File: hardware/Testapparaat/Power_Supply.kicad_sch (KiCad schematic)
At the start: 2 parts

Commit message: -enh Made the schematic for the main unit almost complete :)
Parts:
- removed BT?: Li-battery 3,5-4,2V, symbol Device:Battery
- removed M?: TP4056_Module, testapparaat_footprint:4056E_LiIon_Charger, symbol testapparaat_symbols:TP4056_Module
- added BT1: NIMH_CELL_AA_1, symbol Device:Battery_Cell
- added BT2: NIMH_CELL_AA_8, symbol Device:Battery_Cell
- added BT3: NIMH_CELL_AA_2, symbol Device:Battery_Cell
- added BT4: NIMH_CELL_AA_7, symbol Device:Battery_Cell
- added BT5: NIMH_CELL_AA_6, symbol Device:Battery_Cell
- added BT6: NIMH_CELL_AA_3, symbol Device:Battery_Cell
- added BT7: NIMH_CELL_AA_4, symbol Device:Battery_Cell
- added BT8: NIMH_CELL_AA_5, symbol Device:Battery_Cell
- added C2: 220u, symbol Device:C_Polarized
- added C3: 1u, symbol Device:C
- added C4, C5: 100n, symbol Device:C
- added C6, C7: 2.2u, symbol Device:C
- added C8, C9: 10u, symbol Device:C_Polarized
- added F1: F2.5A GLASS, symbol Device:Fuse
- added L1: 4.7uH, symbol Device:L
- added L2: 3.3uH, symbol Device:L
- added PS1, PS2: LMR50410YFQDBVRQ1, LMR50410YFQDBVRQ1:SOT95P280X145-6N, symbol LMR50410YFQDBVRQ1:LMR50410YFQDBVRQ1
- added R10: 20k, symbol Device:R
- added R6: 100k, symbol Device:R
- added R7: 91k, symbol Device:R
- added R8: 22k, symbol Device:R
- added R9: 43k, symbol Device:R
- added SW2: on/off switch, symbol Switch:SW_Push_SPDT
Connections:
- net 3.3V_OUT: now also C9.1, L2.2, R9.1
- net 5V_OUT: now also C8.1, L1.2, R7.1
- new net: PS1.3 (FB), R7.2, R8.1
- new net: BT6.1 (+), BT7.1 (+)
- new net: BT3.1 (+), BT6.2 (-)
- new net: PS2.3 (FB), R10.1, R9.2
- new net: BT2.1 (+), C2.1, F1.2
- new net: BT4.2 (-), BT5.1 (+)
- new net: BT5.2 (-), BT8.1 (+)
- new net: C4.1, L1.1, PS1.6 (SW)
- new net: BT7.2 (-), BT8.2 (-)
- new net: C4.2, PS1.1 (CB)
- new net: BT1.1 (+), BT3.2 (-)
- new net: BT2.2 (-), BT4.1 (+)
- new net: C5.2, PS2.1 (CB)
- new net: C5.1, L2.1, PS2.6 (SW)
- new net BATT_OUT+: C6.1, C7.1, F1.1, PS1.5 (VIN), PS2.5 (VIN), SW2.1 (A)
- new net BATT_OUT-: BT1.2 (-), C2.2, C3.2, C6.2, C7.2, C8.2, C9.2, PS1.2 (GND), PS2.2 (GND), R10.2, R6.2, R8.2, SW2.3 (C)
- new net REG_EN: C3.1, PS1.4 (EN), PS2.4 (EN), R6.1, SW2.2 (B)
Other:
- note added: "RFBT = ((Vout-Vref)/Vref)*RFBB RFBB = 20k (gaf een goede verhouding) Vref = 1v (datasheet LMR) RFBT = ((3.2-1)/1)*20000 = 44k -> 43k gekozen"
- note added: "RFBT = ((Vout-Vref)/Vref)*RFBB RFBB = 22k (gaf een goede verhouding) Vref = 1v (datasheet LMR) RFBT = ((5.2-1)/1)*20000=92,4k -> 91k gekozen"

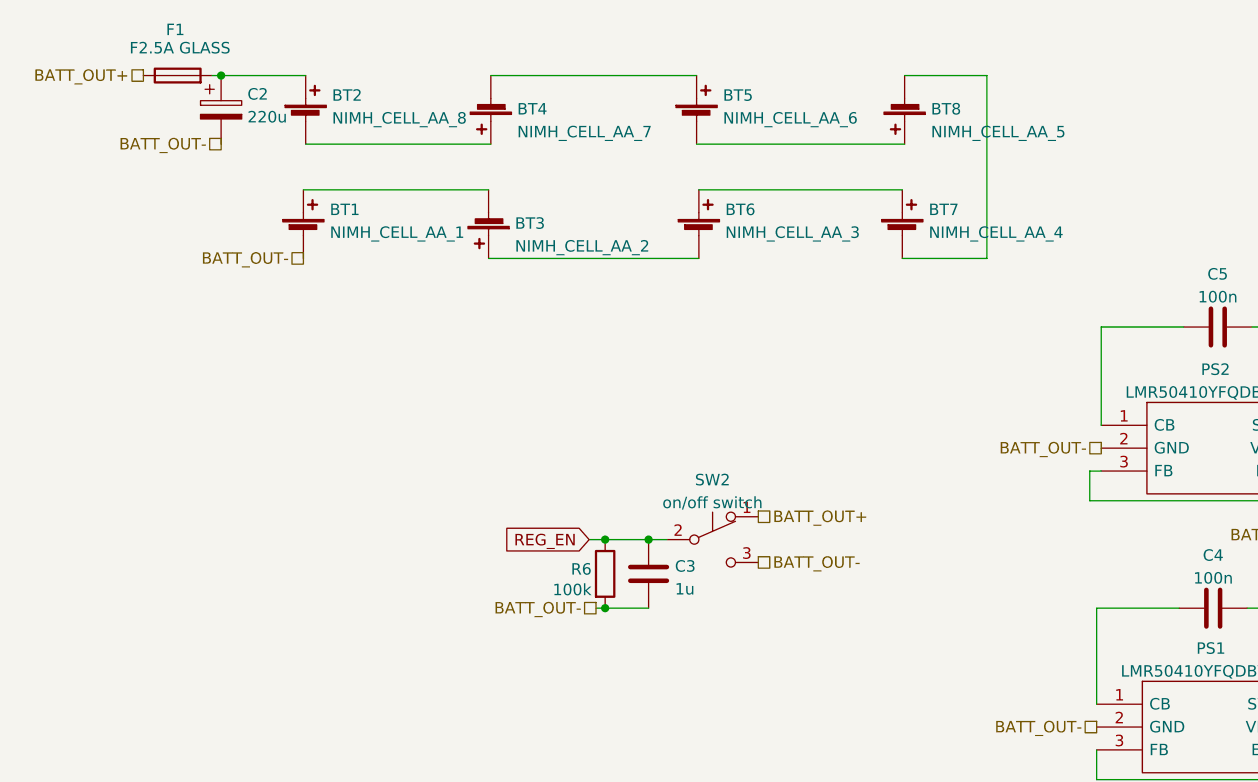
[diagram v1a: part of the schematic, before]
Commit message: -enh Noodstop is now hardware controlled
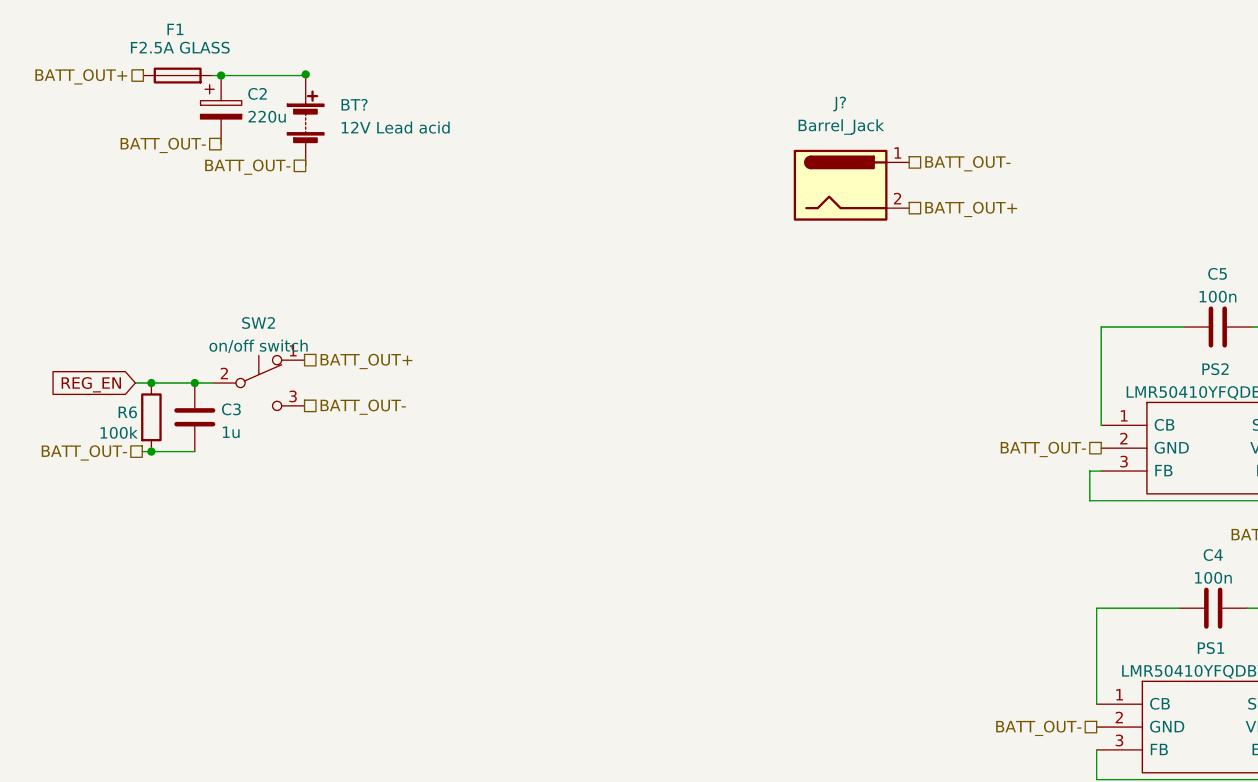
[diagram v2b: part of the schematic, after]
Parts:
- removed BT1: NIMH_CELL_AA_1, symbol Device:Battery_Cell
- removed BT2: NIMH_CELL_AA_8, symbol Device:Battery_Cell
- removed BT3: NIMH_CELL_AA_2, symbol Device:Battery_Cell
- removed BT4: NIMH_CELL_AA_7, symbol Device:Battery_Cell
- removed BT5: NIMH_CELL_AA_6, symbol Device:Battery_Cell
- removed BT6: NIMH_CELL_AA_3, symbol Device:Battery_Cell
- removed BT7: NIMH_CELL_AA_4, symbol Device:Battery_Cell
- removed BT8: NIMH_CELL_AA_5, symbol Device:Battery_Cell
- added BT?: 12V Lead acid, symbol Device:Battery
- added J?: Barrel_Jack, symbol Connector:Barrel_Jack
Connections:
- net BATT_OUT+: now also J?.2
- net BATT_OUT-: now also BT?.2 (-), J?.1
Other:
- moved on the sheet: C3, R6, SW2

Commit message: -enh made some changes to schematic and assigned fp
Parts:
- added D8: 1N5401, Diode_THT:D_DO-201AD_P15.24mm_Horizontal, symbol Diode:1N5401
- added J10: B-, TestPoint:TestPoint_Plated_Hole_D2.0mm, symbol Connector:Conn_01x01_Female
- added J9: B+, TestPoint:TestPoint_Plated_Hole_D2.0mm, symbol Connector:Conn_01x01_Female
- C2: footprint (none) -> Capacitor_THT:C_Radial_D10.0mm_H12.5mm_P5.00mm
- C3, C4, C5, C6, C7, C8, C9: footprint (none) -> Capacitor_SMD:C_0603_1608Metric_Pad1.08x0.95mm_HandSolder
- F1: footprint (none) -> Fuse:Fuseholder_Blade_ATO_Littelfuse_Pudenz_2_Pin
- J8: renamed from J?; footprint (none) -> Connector_BarrelJack:BarrelJack_Wuerth_6941xx301002
- L1, L2: footprint (none) -> Inductor_SMD:L_Bourns-SRU8028_8.0x8.0mm
- R10, R6, R7, R8, R9: footprint (none) -> Resistor_SMD:R_0603_1608Metric_Pad0.98x0.95mm_HandSolder
- SW2: footprint (none) -> Button_Switch_THT:SW_Slide_1P2T_CK_OS102011MS2Q
- gave numbers to parts that had none: 1
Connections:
- net BATT_OUT+: now also D8.1 (K); no longer J8.2
- net BATT_OUT-: now also J8.2, J10.1 (Pin_1); no longer J8.1
- net at C2.1, F1.2: now also J9.1 (Pin_1)
- new net: D8.2 (A), J8.1

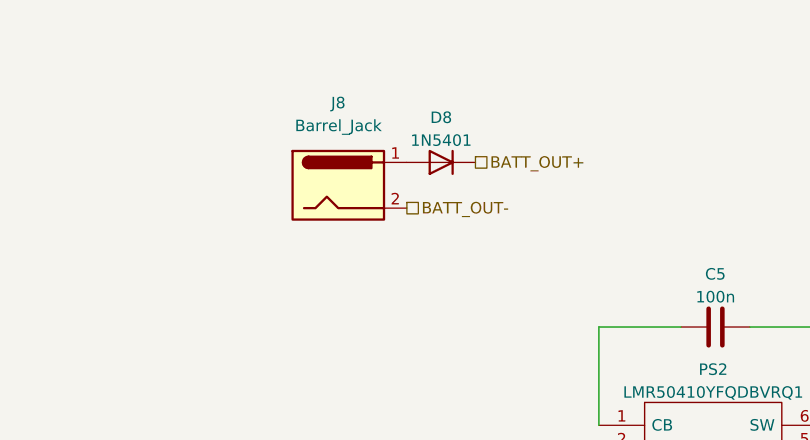
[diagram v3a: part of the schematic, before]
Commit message: -enh add seperate schematic and pcb for io ports/slots
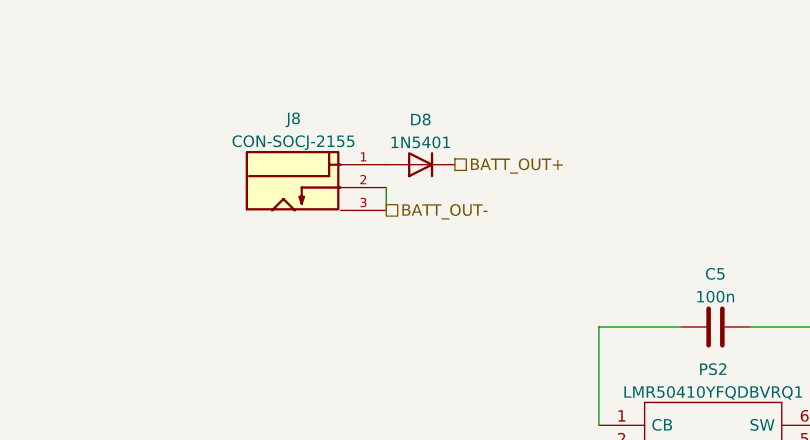
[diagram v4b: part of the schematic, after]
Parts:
- removed J8: Barrel_Jack, Connector_BarrelJack:BarrelJack_Wuerth_6941xx301002, symbol Connector:Barrel_Jack
- added J8: CON-SOCJ-2155, Barrel_jack:GRAVITECH_CON-SOCJ-2155, symbol Barrel_jack:CON-SOCJ-2155
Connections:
- net BATT_OUT-: now also J8.2, J8.3
- net at D8.2 (A): now also J8.1
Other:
- moved on the sheet: D8
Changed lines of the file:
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@@
+    (stroke (width 0) (type default) (color 0 0 0 0))
+  )
+  (wire (pts (xy 121.92 30.988) (xy 121.92 33.528))
     (stroke (width 0) (type default) (color 0 0 0 0))
   )
@@
     (effects (font (size 1.27 1.27)) (justify right))
   )
-  (hierarchical_label "BATT_OUT+" (shape passive) (at 131.826 28.194 0)
+  (hierarchical_label "BATT_OUT+" (shape passive) (at 129.54 28.448 0)
     (effects (font (size 1.27 1.27)) (justify left))
   )
@@
     (effects (font (size 1.27 1.27)) (justify left))
   )
-  (hierarchical_label "BATT_OUT-" (shape passive) (at 124.206 33.274 0)
+  (hierarchical_label "BATT_OUT-" (shape passive) (at 121.92 33.528 0)
     (effects (font (size 1.27 1.27)) (justify left))
   )
@@
     (pin "1")
   )
-  (symbol (lib_id "Diode:1N5401") (at 128.016 28.194 180) (unit 1)
-    (in_bom yes) (on_board yes) (fields_autoplaced)
-    (property "Reference" "D8" (id 0) (at 128.016 23.2242 0))
-    (property "Value" "1N5401" (id 1) (at 128.016 25.7611 0))
-    (property "Footprint" "Diode_THT:D_DO-201AD_P15.24mm_Horizontal" (id 2) (at 128.016 23.749 0)
-      (effects (font (size 1.27 1.27)) hide)
-    )
-    (property "Datasheet" "http://www.vishay.com/docs/88516/1n5400.pdf" (id 3) (at 128.016 28.194 0)
-      (effects (font (size 1.27 1.27)) hide)
-    )
-    (pin "1")
-    (pin "2")
+  (symbol (lib_id "Diode:1N5401") (at 125.73 28.448 180) (unit 1)
+    (in_bom yes) (on_board yes) (fields_autoplaced)
+    (property "Reference" "D8" (id 0) (at 125.73 23.4782 0))
+    (property "Value" "1N5401" (id 1) (at 125.73 26.0151 0))
+    (property "Footprint" "Diode_THT:D_DO-201AD_P15.24mm_Horizontal" (id 2) (at 125.73 24.003 0)
+      (effects (font (size 1.27 1.27)) hide)
+    )
+    (property "Datasheet" "http://www.vishay.com/docs/88516/1n5400.pdf" (id 3) (at 125.73 28.448 0)
+      (effects (font (size 1.27 1.27)) hide)
+    )
+    (pin "1")
+    (pin "2")
+  )
+  (symbol (lib_id "Barrel_jack:CON-SOCJ-2155") (at 111.76 30.988 0) (unit 1)
+    (in_bom yes) (on_board yes) (fields_autoplaced)
+    (property "Reference" "J8" (id 0) (at 111.633 23.3512 0))
+    (property "Value" "CON-SOCJ-2155" (id 1) (at 111.633 25.8881 0))
+    (property "Footprint" "Barrel_jack:GRAVITECH_CON-SOCJ-2155" (id 2) (at 111.76 30.988 0)
+      (effects (font (size 1.27 1.27)) (justify left bottom) hide)
+    )
+    (property "Datasheet" "" (id 3) (at 111.76 30.988 0)
+      (effects (font (size 1.27 1.27)) (justify left bottom) hide)
+    )
+    (property "STANDARD" "Manufacturer Recommendations" (id 4) (at 111.76 30.988 0)
+      (effects (font (size 1.27 1.27)) (justify left bottom) hide)
+    )
+    (property "PARTREV" "NA" (id 5) (at 111.76 30.988 0)
+      (effects (font (size 1.27 1.27)) (justify left bottom) hide)
+    )
+    (property "MANUFACTURER" "Gravitech" (id 6) (at 111.76 30.988 0)
+      (effects (font (size 1.27 1.27)) (justify left bottom) hide)
+    )
+    (property "MAXIMUM_PACKAGE_HEIGHT" "11.1 mm" (id 7) (at 111.76 30.988 0)
+      (effects (font (size 1.27 1.27)) (justify left bottom) hide)
+    )
+    (pin "1")
+    (pin "2")
+    (pin "3")
   )
   (symbol (lib_id "Connector:Conn_01x01_Female") (at 62.23 18.542 0) (unit 1)
@@
       (effects (font (size 1.27 1.27)) hide)
     )
-    (pin "1")
-    (pin "2")
-  )
-  (symbol (lib_id "Connector:Barrel_Jack") (at 116.586 30.734 0) (unit 1)
-    (in_bom yes) (on_board yes) (fields_autoplaced)
-    (property "Reference" "J8" (id 0) (at 116.586 21.59 0))
-    (property "Value" "Barrel_Jack" (id 1) (at 116.586 24.13 0))
-    (property "Footprint" "Connector_BarrelJack:BarrelJack_Wuerth_6941xx301002" (id 2) (at 117.856 31.75 0)
-      (effects (font (size 1.27 1.27)) hide)
-    )
-    (property "Datasheet" "~" (id 3) (at 117.856 31.75 0)
-      (effects (font (size 1.27 1.27)) hide)
-    )

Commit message: -add bom and new schematic
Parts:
- removed C4, C5: 100n, Capacitor_SMD:C_0603_1608Metric_Pad1.08x0.95mm_HandSolder, symbol Device:C
- removed C7: 2.2u, Capacitor_SMD:C_0603_1608Metric_Pad1.08x0.95mm_HandSolder, symbol Device:C
- removed PS1, PS2: LMR50410YFQDBVRQ1, LMR50410YFQDBVRQ1:SOT95P280X145-6N, symbol LMR50410YFQDBVRQ1:LMR50410YFQDBVRQ1
- added D? (x2): SS310, symbol Device:D_Schottky
- added U? (x2): LM2596S-ADJ, Package_TO_SOT_SMD:TO-263-5_TabPin3, symbol Regulator_Switching:LM2596S-ADJ
- C8, C9: value 10u -> 220u
- L1: value 4.7uH -> 68uH
- L2: value 3.3uH -> 68uH
- R10: value 20k -> 1k
- R7: value 91k -> 680
- R8: value 22k -> 220
- R9: value 43k -> 1,6k
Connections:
- net BATT_OUT+: now also U?.1 (VIN), U?.1 (VIN)
- net BATT_OUT-: now also D?.2 (A), D?.2 (A), U?.3 (GND), U?.3 (GND)
- net REG_EN: now also U?.5 (~{ON}/OFF), U?.5 (~{ON}/OFF)
- net at R7.2, R8.1: now also U?.4 (FB)
- net at R10.1, R9.2: now also U?.4 (FB)
- net at L1.1: now also D?.1 (K), U?.2 (OUT)
- net at L2.1: now also D?.1 (K), U?.2 (OUT)
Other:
- note added: "RFBT = RFBB((vout/vref)-1) RFBB = 1k (gaf een goede verhouding) Vref = 1,23v (datasheet LM2596) RFBT = 1k((3,3/1,23)-1)= 1,68k -> 1,6k gekozen"
- note added: "RFBT = RFBB((vout/vref)-1) RFBB = 1k (gaf een goede verhouding) Vref = 1,23v (datasheet LM2596) RFBT = 1k((5/1,23)-1)= 3065R -> 3k gekozen"
- note removed: "RFBT = ((Vout-Vref)/Vref)*RFBB RFBB = 20k (gaf een goede verhouding) Vref = 1v (datasheet LMR) RFBT = ((3.2-1)/1)*20000 = 44k -> 43k gekozen"
- note removed: "RFBT = ((Vout-Vref)/Vref)*RFBB RFBB = 22k (gaf een goede verhouding) Vref = 1v (datasheet LMR) RFBT = ((5.2-1)/1)*20000=92,4k -> 91k gekozen"
- moved on the sheet: C6

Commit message: -enh Made a start at pcb design
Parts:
- removed C6: 2.2u, Capacitor_SMD:C_0603_1608Metric_Pad1.08x0.95mm_HandSolder, symbol Device:C
- removed D8: 1N5401, Diode_THT:D_DO-201AD_P15.24mm_Horizontal, symbol Diode:1N5401
- removed U? (x2): LM2596S-ADJ, Package_TO_SOT_SMD:TO-263-5_TabPin3, symbol Regulator_Switching:LM2596S-ADJ
- added D4: SS310, Diode_SMD:D_SMA_Handsoldering, symbol Device:D_Schottky
- added U10: LM2596S-5, Package_TO_SOT_SMD:TO-263-5_TabPin3, symbol Regulator_Switching:LM2596S-5
- added U11: LM2596S-3.3, Package_TO_SOT_SMD:TO-263-5_TabPin3, symbol Regulator_Switching:LM2596S-3.3
- C8, C9: footprint Capacitor_SMD:C_0603_1608Metric_Pad1.08x0.95mm_HandSolder -> Capacitor_THT:C_Radial_D10.0mm_H12.5mm_P5.00mm
- D1, D2: renamed from D?; footprint (none) -> Diode_SMD:D_SMA_Handsoldering
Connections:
- net REG_EN: now also U10.5 (~{ON}/OFF), U11.5 (~{ON}/OFF)
- net at R7.2, R8.1: now also U10.4 (FB)
- net at R10.1, R9.2: now also U11.4 (FB)
- net at C2.1, F1.2, J9.1 (Pin_1): now also #BT1.1 (+)
- net at D1.1 (K), L1.1: now also U10.2 (OUT)
- net at D2.1 (K), L2.1: now also U11.2 (OUT)
- net at J8.1: now also D4.2 (A)
- net 3.3V_OUT renamed +3.3V
- net 5V_OUT renamed +5V
- net BATT_OUT+ renamed +BATT
- net +BATT: now also D4.1 (K), U10.1 (VIN), U11.1 (VIN)
- net BATT_OUT- renamed GND
- net GND: now also U10.3 (GND), U11.3 (GND)
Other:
- moved on the sheet: C2, F1, J10, J9

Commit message: -enh First look at layout, proposed it to the team
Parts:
- F1: footprint Fuse:Fuseholder_Blade_ATO_Littelfuse_Pudenz_2_Pin -> Fuse:Fuseholder_Littelfuse_100_series_5x20mm
- L1, L2: footprint Inductor_SMD:L_Bourns-SRU8028_8.0x8.0mm -> srr1260:SRR1260-680M
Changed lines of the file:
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@@
     (property "Reference" "F1" (id 0) (at 67.564 13.462 90))
     (property "Value" "F2.5A GLASS" (id 1) (at 67.056 15.494 90))
-    (property "Footprint" "Fuse:Fuseholder_Blade_ATO_Littelfuse_Pudenz_2_Pin" (id 2) (at 67.31 20.32 90)
+    (property "Footprint" "Fuse:Fuseholder_Littelfuse_100_series_5x20mm" (id 2) (at 67.31 20.32 90)
       (effects (font (size 1.27 1.27)) hide)
     )
@@
     (property "Reference" "L1" (id 0) (at 177.546 84.1842 90))
     (property "Value" "68uH" (id 1) (at 177.546 86.7211 90))
-    (property "Footprint" "Inductor_SMD:L_Bourns-SRU8028_8.0x8.0mm" (id 2) (at 177.546 88.392 0)
+    (property "Footprint" "srr1260:SRR1260-680M" (id 2) (at 177.546 88.392 0)
       (effects (font (size 1.27 1.27)) hide)
     )
@@
     (property "Reference" "L2" (id 0) (at 177.8 53.1962 90))
     (property "Value" "68uH" (id 1) (at 177.8 55.7331 90))
-    (property "Footprint" "Inductor_SMD:L_Bourns-SRU8028_8.0x8.0mm" (id 2) (at 177.8 57.404 0)
-      (effects (font (size 1.27 1.27)) hide)
-    )
+    (property "Footprint" "srr1260:SRR1260-680M" (id 2) (at 177.8 57.404 0)
+      (effects (font (size 1.27 1.27)) hide)
+    )

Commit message: -enh drc check
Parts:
- L1, L2: footprint srr1260:SRR1260-680M -> Inductor_SMD:L_Bourns_SRR1260
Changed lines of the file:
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@@
     (property "Reference" "L1" (id 0) (at 177.546 84.1842 90))
     (property "Value" "68uH" (id 1) (at 177.546 86.7211 90))
-    (property "Footprint" "srr1260:SRR1260-680M" (id 2) (at 177.546 88.392 0)
+    (property "Footprint" "Inductor_SMD:L_Bourns_SRR1260" (id 2) (at 177.546 88.392 0)
       (effects (font (size 1.27 1.27)) hide)
     )
@@
     (property "Reference" "L2" (id 0) (at 177.8 53.1962 90))
     (property "Value" "68uH" (id 1) (at 177.8 55.7331 90))
-    (property "Footprint" "srr1260:SRR1260-680M" (id 2) (at 177.8 57.404 0)
-      (effects (font (size 1.27 1.27)) hide)
-    )
+    (property "Footprint" "Inductor_SMD:L_Bourns_SRR1260" (id 2) (at 177.8 57.404 0)
+      (effects (font (size 1.27 1.27)) hide)
+    )
